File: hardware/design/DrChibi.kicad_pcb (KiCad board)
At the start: 4 copper layers, 141 x 14 mm, 230 parts, among them P1 CONN_02X05, P2 PAD_SMD, P3 IN+, P4 IN-, P5 CONN_01X04, U1 STM32F40X_LQFP64, U2 ISO1050, X1 MINI-USB-SHIELD-32005-201, X2 8MHz 10ppm

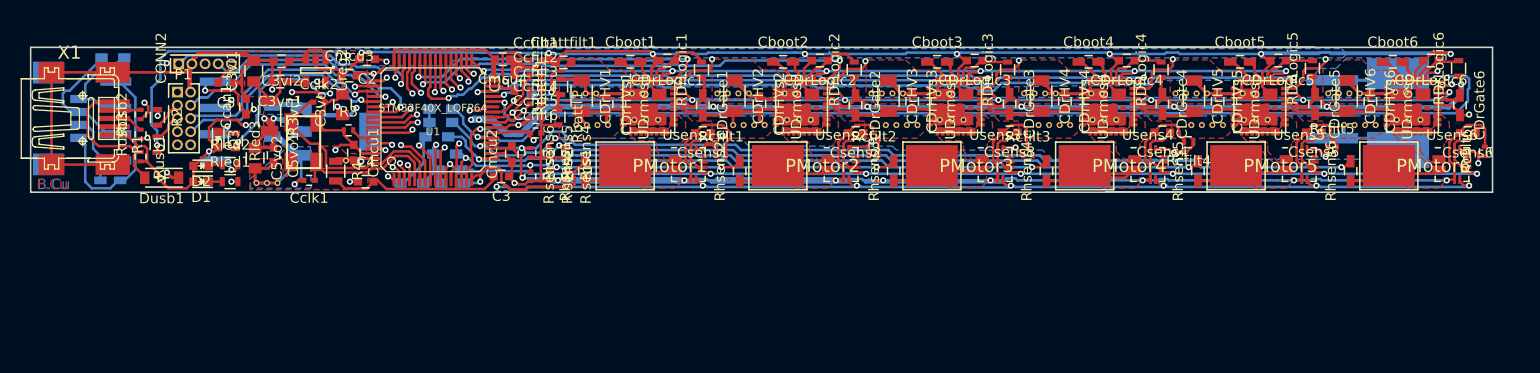
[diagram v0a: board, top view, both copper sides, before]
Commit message: Added mounting holes
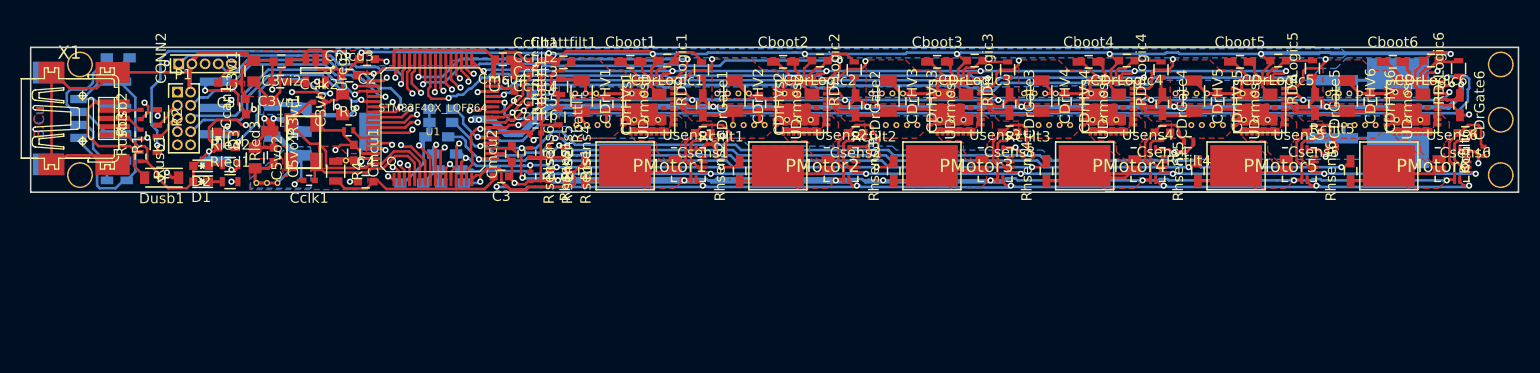
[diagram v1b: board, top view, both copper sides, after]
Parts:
- added REF**: VIA-0.6mm, Pads:VIA-0.6mm, F.Cu at (176.3, 94.7)
- added REF**: VIA-0.6mm, Pads:VIA-0.6mm, F.Cu at (39.3, 94.7)
- added REF**: VIA-0.6mm, Pads:VIA-0.6mm, F.Cu at (176.3, 100.0)
- added REF**: VIA-0.6mm, Pads:VIA-0.6mm, F.Cu at (176.3, 105.3)
- added REF**: VIA-0.6mm, Pads:VIA-0.6mm, F.Cu at (39.3, 105.3)
- moved Ccan2 0.63 mm to (42.8, 105.8)
- moved Rcan1 0.51 mm to (42.9, 94.0)
- moved Csens6 0.24 mm to (172.9, 101.3)
- moved Rcfilt6 0.13 mm to (174.6, 103.0)
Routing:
- net /CAN bus transceiver/CANL: track 12.5 -> 14.7 mm
- net GND: track 828.2 -> 830.3 mm
- net /CAN bus transceiver/CANH: track 10.5 -> 12.0 mm
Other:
- board size 141 x 14 mm -> 143.5 x 14 mm

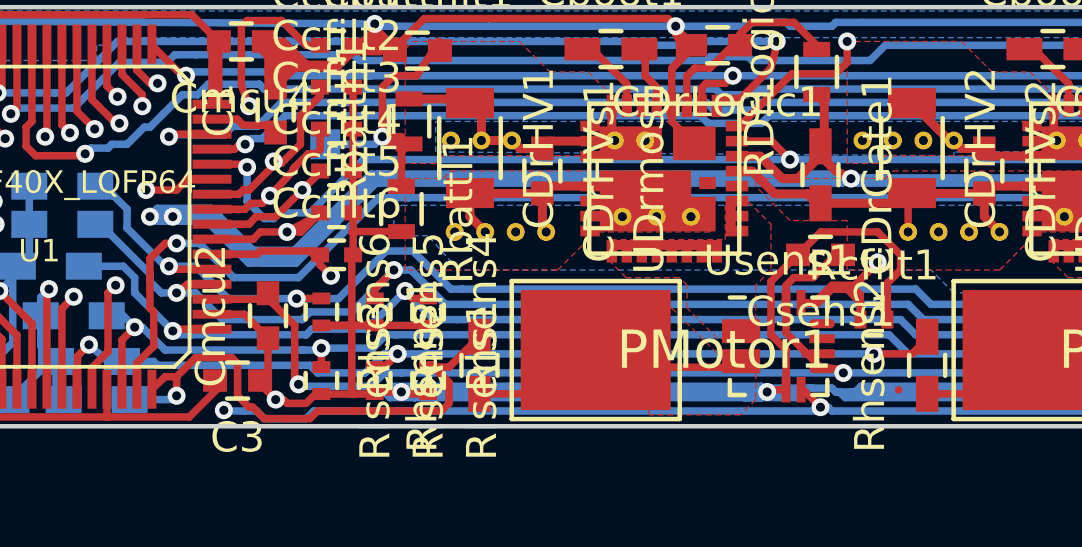
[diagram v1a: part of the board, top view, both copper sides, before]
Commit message: Fixed solder stop for some pads
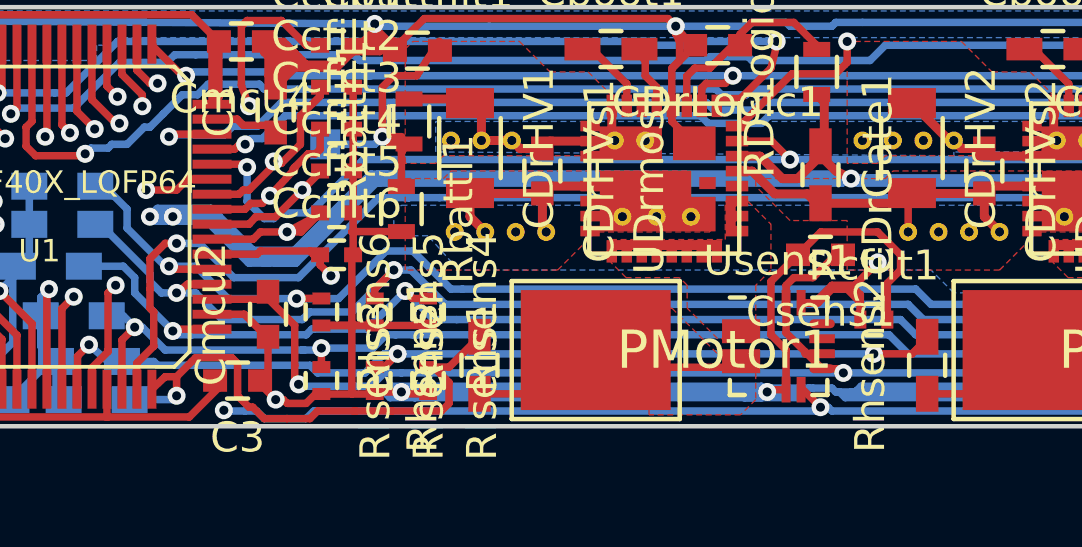
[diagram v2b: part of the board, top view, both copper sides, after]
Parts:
- moved Cmcu2 0.05 mm to (80.9, 103.3)

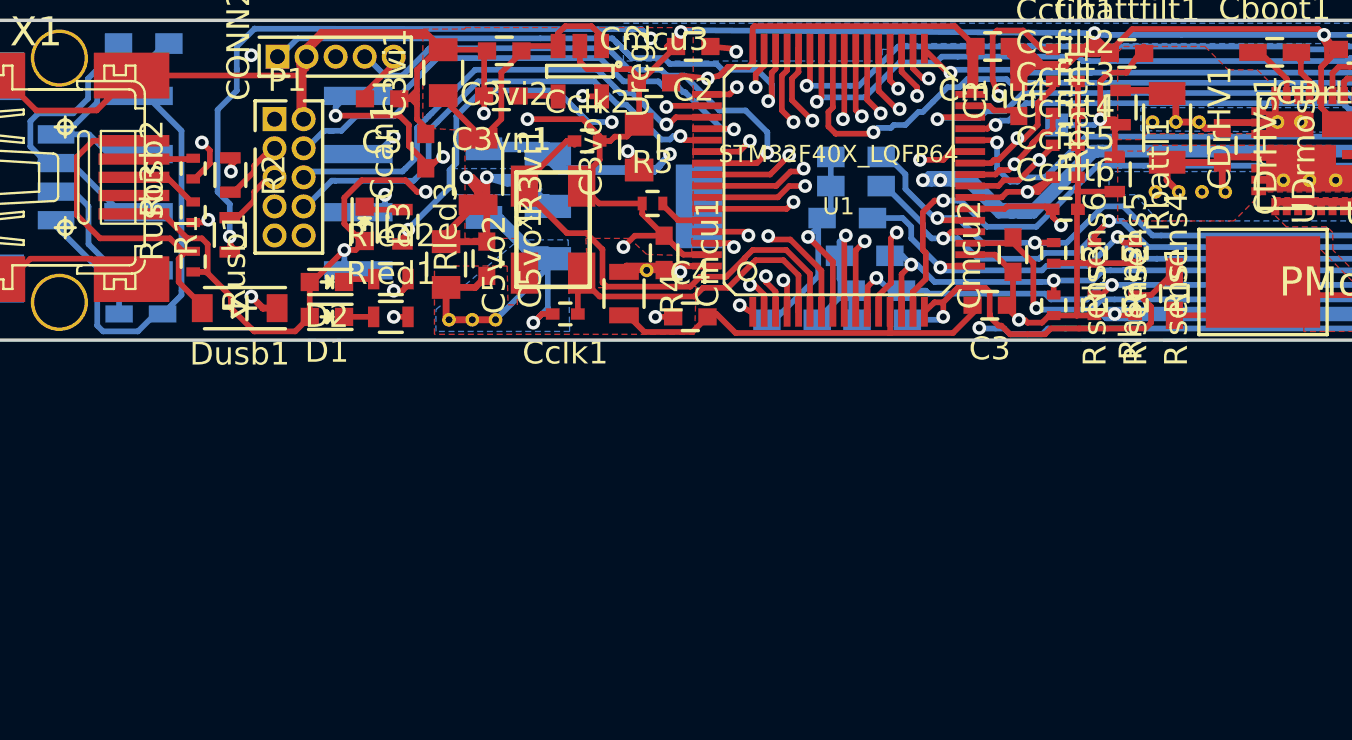
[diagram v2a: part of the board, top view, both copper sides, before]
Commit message: Added the 5V regulator LTM8020 to the schematic.
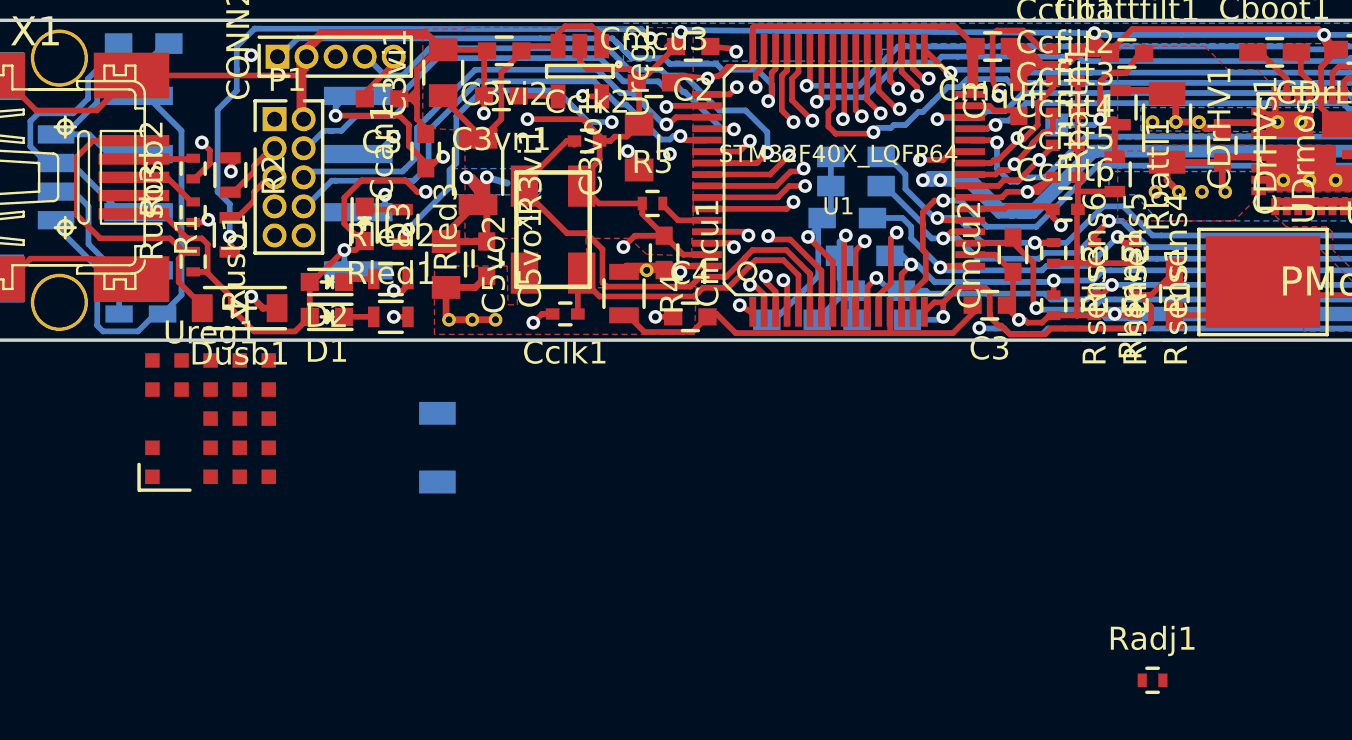
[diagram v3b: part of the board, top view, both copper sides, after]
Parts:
- added Radj1: 165R, Resistors_SMD:R_0402, F.Cu at (87.0, 121.8)
- Ureg1: value NCP1117ST50T3G -> LTM8020; footprint TO_SOT_Packages_SMD:SOT-223 -> Regulators_User:Housings_LGA_21_6.25x6.25mm; moved to F.Cu
- moved Ureg1 20.3 mm to (45.9, 110.4), turned to 0 degrees
- moved Cpwr1 11.7 mm to (55.8, 111.7)
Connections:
- Ureg1 pad 1: GND -> +24V
- Ureg1 pad 3: +24V -> GND
- Ureg1 pad 4: (no net) -> +24V
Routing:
- net +24V: track 179.6 -> 158.4 mm
- net GND: track 830.3 -> 816.6 mm
- net +5V: track 330.4 -> 325.3 mm

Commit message: Removed LED3 to gain some space for the 5V voltage regulator
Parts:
- removed D3: LED, LEDs:LED_0603
- removed the REF**11 at (56.3, 106.1)
- removed Rled3: 100, Resistors_SMD:R_0603
- moved Radj1 21.6 mm to (66.7, 114.5)
- moved Ureg1 16.5 mm to (62.1, 113.0)
- moved R1 5.91 mm to (45.1, 96.7), turned to 270 degrees
- moved C5 5.46 mm to (47.9, 96.4), turned to 0 degrees
- moved R2 5.43 mm to (45.9, 94.4), turned to 180 degrees
- moved P1 1.94 mm to (47.0, 98.3)
- moved C5vo2 1.40 mm to (56.1, 105.1)
- moved Rled2 0.15 mm to (53.7, 104.5)
- moved Rled1 0.13 mm to (53.7, 106.1)
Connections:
- U1 pad 50: /MCU/LED3 -> (no net)
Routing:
- net /MCU/LED3: track 18.9 -> 0.00 mm, vias 3 -> 0
- net GND: track 816.6 -> 809.1 mm
- net /MCU/I2C_SDA: track 33.2 -> 26.0 mm
- net /MCU/USART6_RX: track 43.7 -> 37.2 mm, vias 3 -> 2
- net /MCU/PWM_IN1: track 40.0 -> 33.6 mm
- net /MCU/USART6_TX: track 42.0 -> 37.2 mm, vias 2 -> 1
- net /MCU/I2C_SCL: track 32.0 -> 27.6 mm
- net Net-(P1-Pad3): track 2.91 -> 0.00 mm
- net Net-(P1-Pad5): track 2.59 -> 0.00 mm
- net /MCU/USART6_CK: track 36.3 -> 34.1 mm
- net NRST: track 31.0 -> 29.0 mm
- net +5V: track 325.3 -> 323.5 mm
- net Net-(D3-Pad1): track 1.70 -> 0.00 mm
- net /MCU/SPI3_MOSI: track 22.0 -> 20.3 mm
- net /MCU/SPI3_MISO: track 23.5 -> 22.3 mm

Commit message: Do DRC check!
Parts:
- added REF**11: VIA-0.6mm, Pads:VIA-0.6mm, F.Cu at (52.1, 99.7)
- added REF**11: VIA-0.6mm, Pads:VIA-0.6mm, F.Cu at (54.5, 106.3)
- added REF**11: VIA-0.6mm, Pads:VIA-0.6mm, F.Cu at (56.4, 106.2)
- Cpwr1: value 10u,35V -> 4.7u,35V; footprint Capacitors_SMD:C_1206 -> Capacitors_SMD:C_0805; moved to F.Cu
- D1, D2: footprint LEDs:LED_0603 -> LEDs:LED_0402
- R3vi1: footprint Resistors_SMD:R_1206 -> Resistors_SMD:R_0805
- Rled1, Rled2: footprint Resistors_SMD:R_0603 -> Resistors_SMD:R_0402
- moved Radj1 15.8 mm to (56.9, 102.0)
- moved Ureg1 15.7 mm to (52.7, 100.4)
- moved C5vo1 8.21 mm to (53.6, 96.4), turned to 0 degrees
- moved Ccan1 7.96 mm to (47.6, 96.4), turned to 180 degrees
- moved Cpwr1 7.27 mm to (54.2, 104.6), turned to 180 degrees
- moved C5 2.67 mm to (50.6, 96.4)
- moved Rled2 2.29 mm to (51.4, 104.6), turned to 270 degrees
- moved REF**11 1.80 mm to (55.5, 106.3)
- moved C5vo2 1.40 mm to (57.5, 104.9)
- moved Rled1 1.40 mm to (52.3, 106.2)
- moved D2 0.90 mm to (50.1, 104.6), turned to 270 degrees
- moved REF**11 0.77 mm to (59.1, 106.2)
- moved D1 0.68 mm to (50.3, 106.2)
- moved R3vi1 0.14 mm to (57.7, 99.7)
- moved Dusb1 0.13 mm to (47.0, 105.6)
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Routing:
- net GND: track 809.1 -> 858.5 mm, vias 26 -> 25
- net +24V: track 158.4 -> 180.9 mm, vias 1 -> 2
- net +5V: track 323.5 -> 340.6 mm, vias 11 -> 12
- net /MCU/I2C_SDA: track 26.0 -> 34.9 mm
- net /MCU/PWM_IN1: track 33.6 -> 41.1 mm
- net Net-(P1-Pad3): track 0.00 -> 6.26 mm
- net /MCU/I2C_SCL: track 27.6 -> 33.5 mm
- net Net-(P1-Pad5): track 0.00 -> 5.73 mm, vias 0 -> 1
- net /MCU/SPI3_MOSI: track 20.3 -> 24.9 mm
- net /MCU/SPI3_MISO: track 22.3 -> 26.0 mm
- net NRST: track 29.0 -> 32.6 mm
- net /MCU/SPI3_SCK: track 21.1 -> 24.2 mm
- net /MCU/USART6_CK: track 34.1 -> 37.1 mm
- net /CAN bus transceiver/CAN_RX: track 21.5 -> 24.2 mm
- net +3V3: track 227.1 -> 229.8 mm, vias 14 -> 13
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- added copper zone on F.Cu, net +5V
- added copper zone on In1.Cu, net +5V

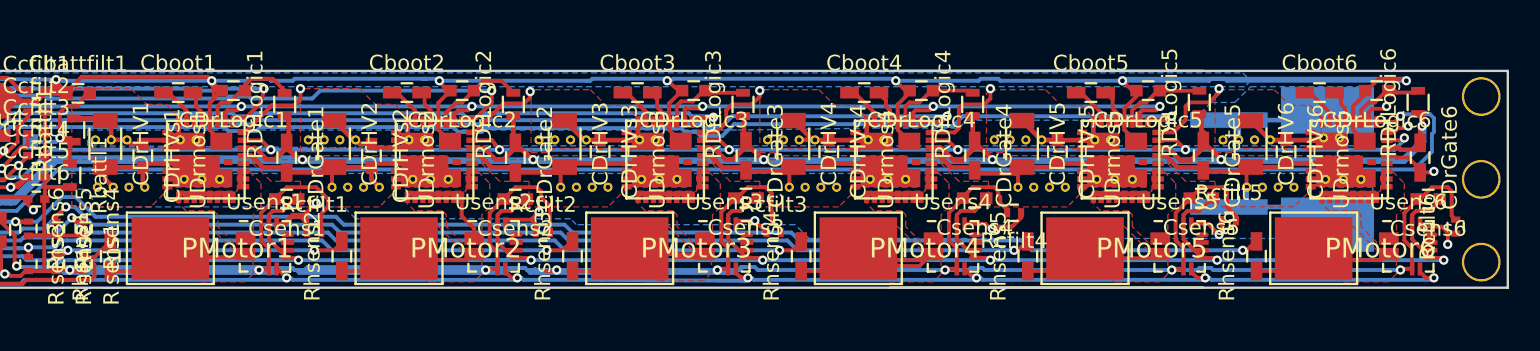
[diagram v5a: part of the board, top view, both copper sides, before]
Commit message: Added pullup resistor for THWn. Fixed some not connected parts warnings.
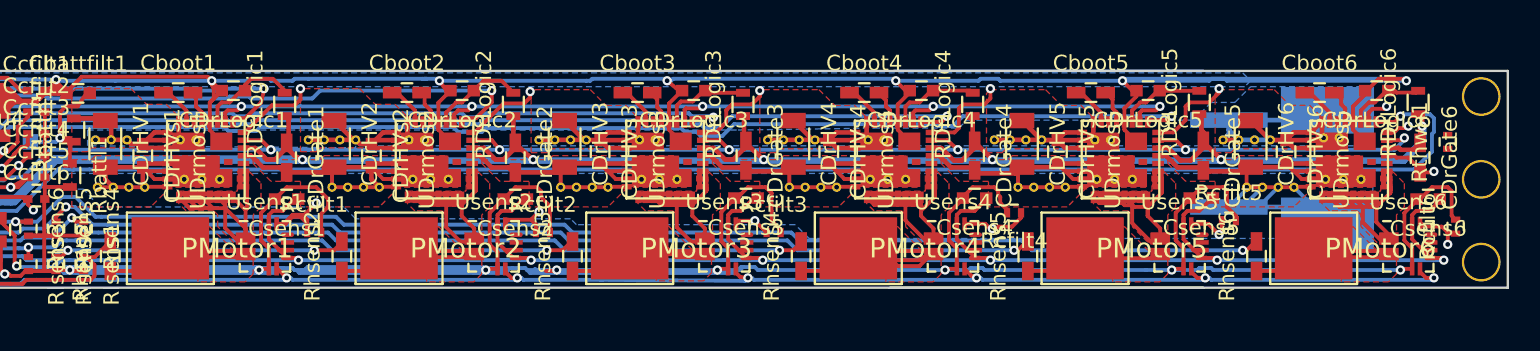
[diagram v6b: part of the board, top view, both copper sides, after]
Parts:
- added Rthwn1: 2k7, Resistors_SMD:R_0402, F.Cu at (174.1, 97.6)
- R3: value R/DNP -> 2k7/DNP
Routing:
- net GND: track 858.5 -> 943.0 mm
- net +24V: track 180.9 -> 230.6 mm
- net Net-(UDrmos3-Pad16): track 0.00 -> 23.6 mm
- net Net-(UDrmos6-Pad16): track 0.00 -> 20.2 mm
- net Net-(UDrmos1-Pad16): track 0.00 -> 19.3 mm
- net Net-(UDrmos5-Pad16): track 0.00 -> 18.3 mm
- net Net-(UDrmos4-Pad16): track 0.00 -> 17.3 mm
- net Net-(UDrmos2-Pad16): track 2.57 -> 19.8 mm
- net Net-(PMotor1-Pad1): track 12.0 -> 16.9 mm
- net Net-(PMotor3-Pad1): track 19.0 -> 23.9 mm
- net Net-(PMotor4-Pad1): track 15.1 -> 20.0 mm
- net Net-(PMotor2-Pad1): track 10.3 -> 14.8 mm
- net Net-(PMotor6-Pad1): track 9.73 -> 14.3 mm
